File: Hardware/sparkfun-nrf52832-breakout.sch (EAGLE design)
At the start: 43 parts, among them J5 CORTEX_DEBUGPTH, U1 3.3V, U2 NRF52832, Y1 32MHz, Y2 32.768kHz

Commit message: Schematic cleanup.
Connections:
- removed net N$8: J1.DTR
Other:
- note added: "32.768kHz Crystal (RTC)"
- note added: "Buttons"
- note added: "Close JP2 & JP3 if you're attaching an NFC antenna."
- note added: "Cortex Debug Connector"
- note added: "Ctune (C7/8) = 2/((2*PI*13.56MHz)^2*La) La is inductance of NFC antenna La=1.5uH, Ctune=~180pF La=2.0uH, Ctune=~130pF"
- note added: "JP4 and JP5 enable the RTC on pins 00 and 01."
- note added: "LEDs"
- note added: "NFC Antenna Interface"
- note added: "NFC Tuning Caps"
- note added: "Pin/Supply Headers"
- note added: "Regulator Input Voltage !3.3 - 6V DC!"
- note added: "Serial Program/Debug"
- note added: "Short JP1 to enable powering the nRF52832 via a 3.3V FTDI Basic"
- note added: "Supply Decoupling"
- note added: "Voltage Regulator"
- note added: "nRF52832"
- note added: "nRF52832 Supply Range !1.7 - 3.6V DC!"
- note removed: "Ctune (C7/8) = 2/((2*PI*13.56MHz)^2*La)-4pF La is inductance of NFC antenna La=1.5uH, Ctune=~180pF La=2.0uH, Ctune=~130pF"
- moved on the sheet: C10, C11, C12, C13, C14, C15, C16, C17, C3, C4, C5, C6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

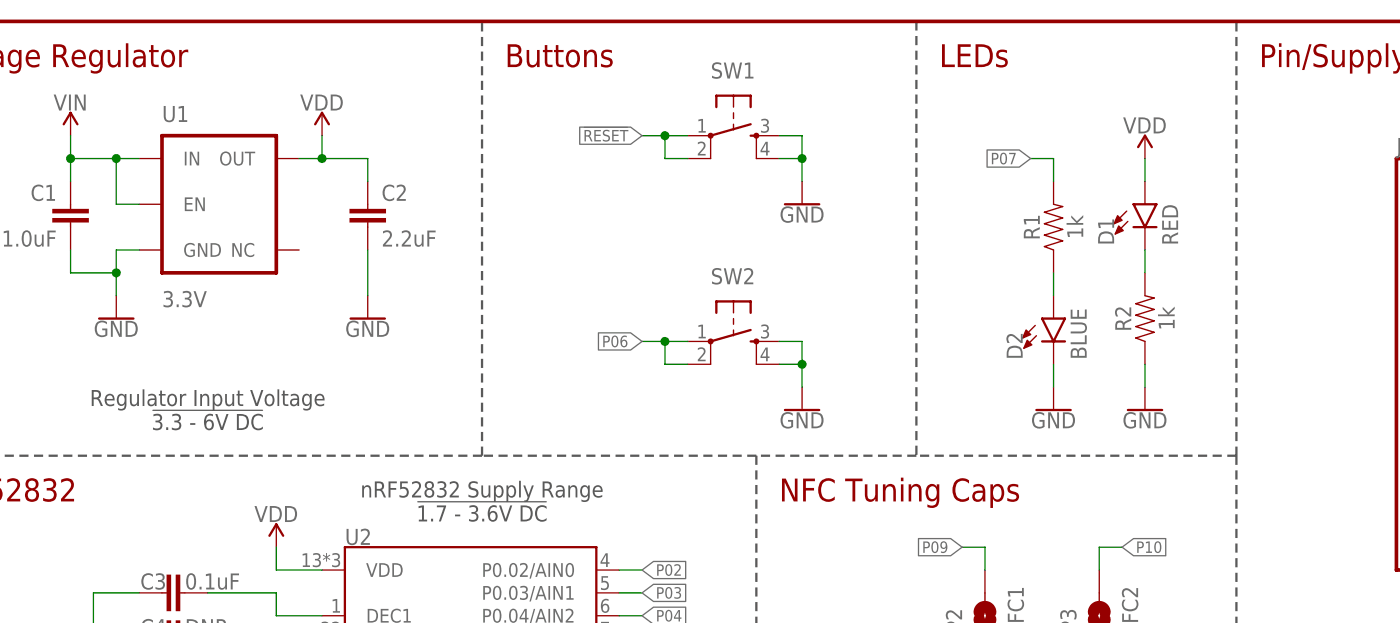
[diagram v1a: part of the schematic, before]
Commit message: Adding cut-jumper to the power LED.
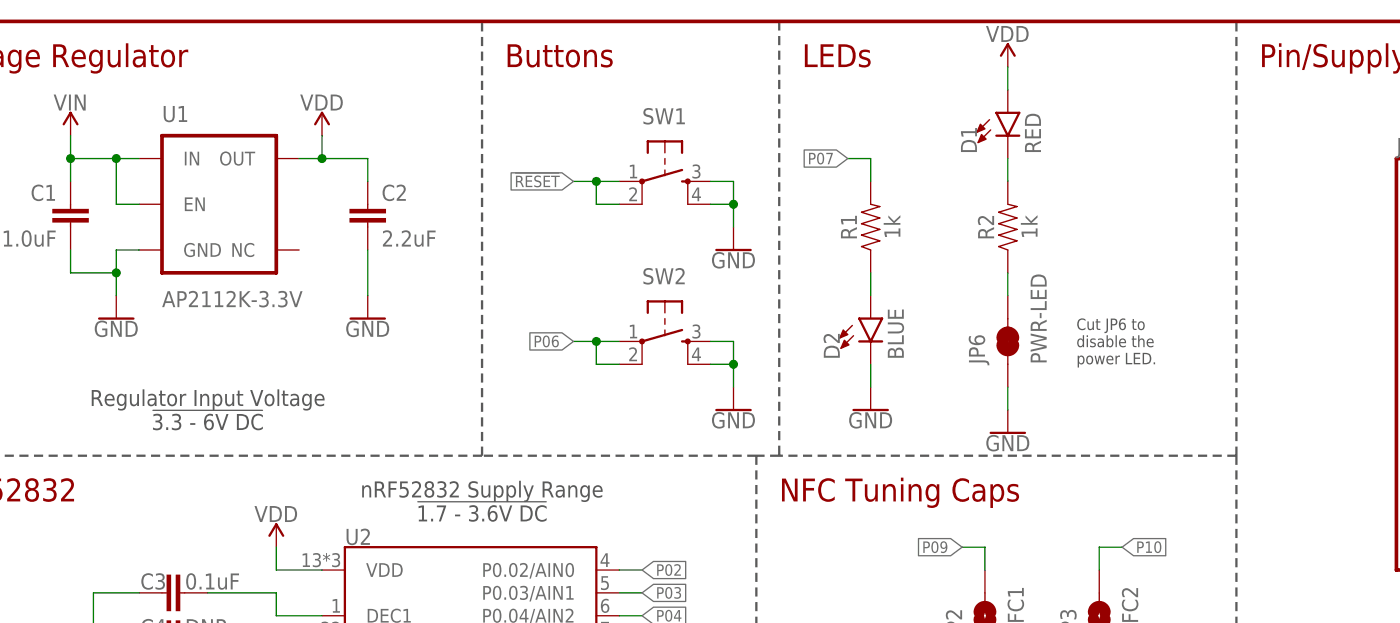
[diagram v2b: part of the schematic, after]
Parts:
- added JP6: PWR-LED, SparkFun-Jumpers:JUMPER-PAD-2-NC_BY_TRACE
- U1: value 3.3V -> AP2112K-3.3V
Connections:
- new net N$1: JP6.2, R2.1
- net GND: now also JP6.1; no longer R2.1
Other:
- note added: "Cut JP6 to disable the power LED."
- moved on the sheet: D1, D2, R1, R2, SW1, SW2

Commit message: Updates after running checklist.
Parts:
- added FD1, FD2: FIDUCIAL1X2, SparkFun-Aesthetics:FIDUCIAL1X2
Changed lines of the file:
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@@
 <part name="LOGO3" library="SparkFun-Aesthetics" deviceset="SFE_LOGO_NAME" device=".1_INCH" value="SFE_LOGO_NAME.1_INCH"/>
 <part name="JP6" library="SparkFun-Jumpers" deviceset="JUMPER-PAD-2-NC_BY_TRACE" device="" value="PWR-LED"/>
+<part name="FD1" library="SparkFun-Aesthetics" deviceset="FIDUCIAL" device="1X2"/>
+<part name="FD2" library="SparkFun-Aesthetics" deviceset="FIDUCIAL" device="1X2"/>
 </parts>
 <sheets>
@@
 <instance part="LOGO3" gate="G$1" x="86.36" y="12.7"/>
 <instance part="JP6" gate="G$1" x="121.92" y="149.86" rot="R90"/>
+<instance part="FD1" gate="G$1" x="243.84" y="20.32"/>
+<instance part="FD2" gate="G$1" x="246.38" y="17.78"/>
 </instances>
 <busses>

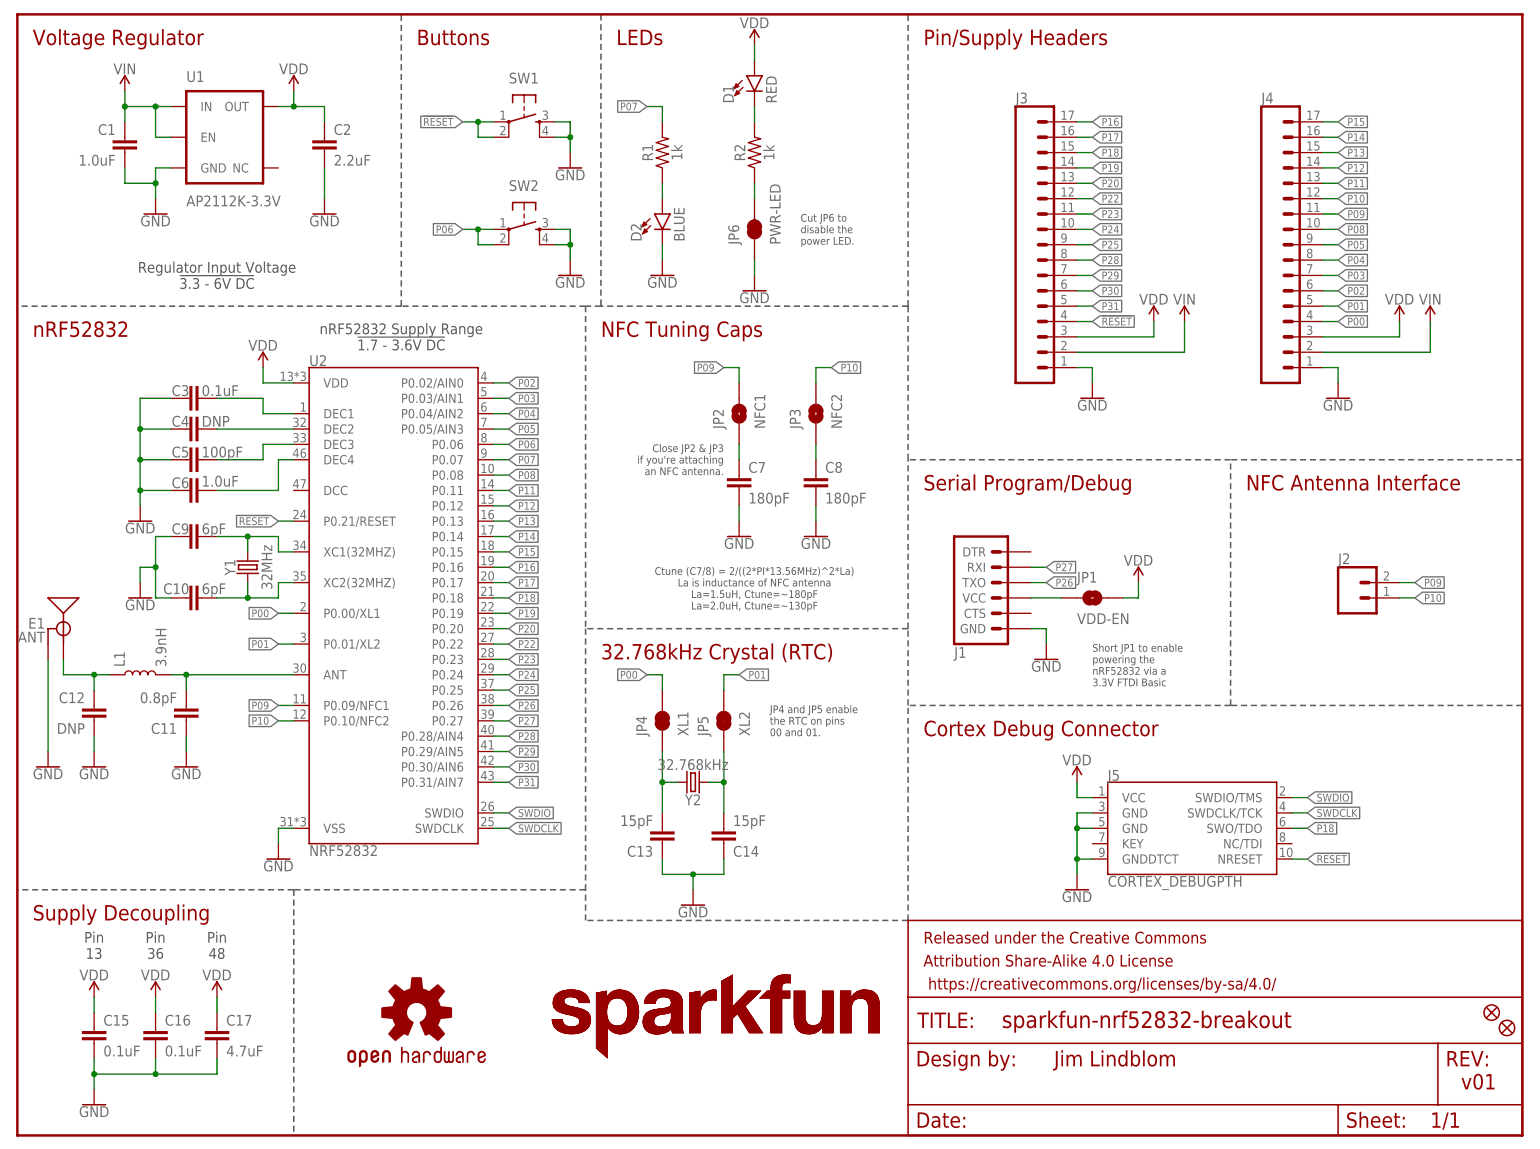
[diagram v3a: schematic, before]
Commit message: Adding test points to swd pins, stubs to NC QFN pins.
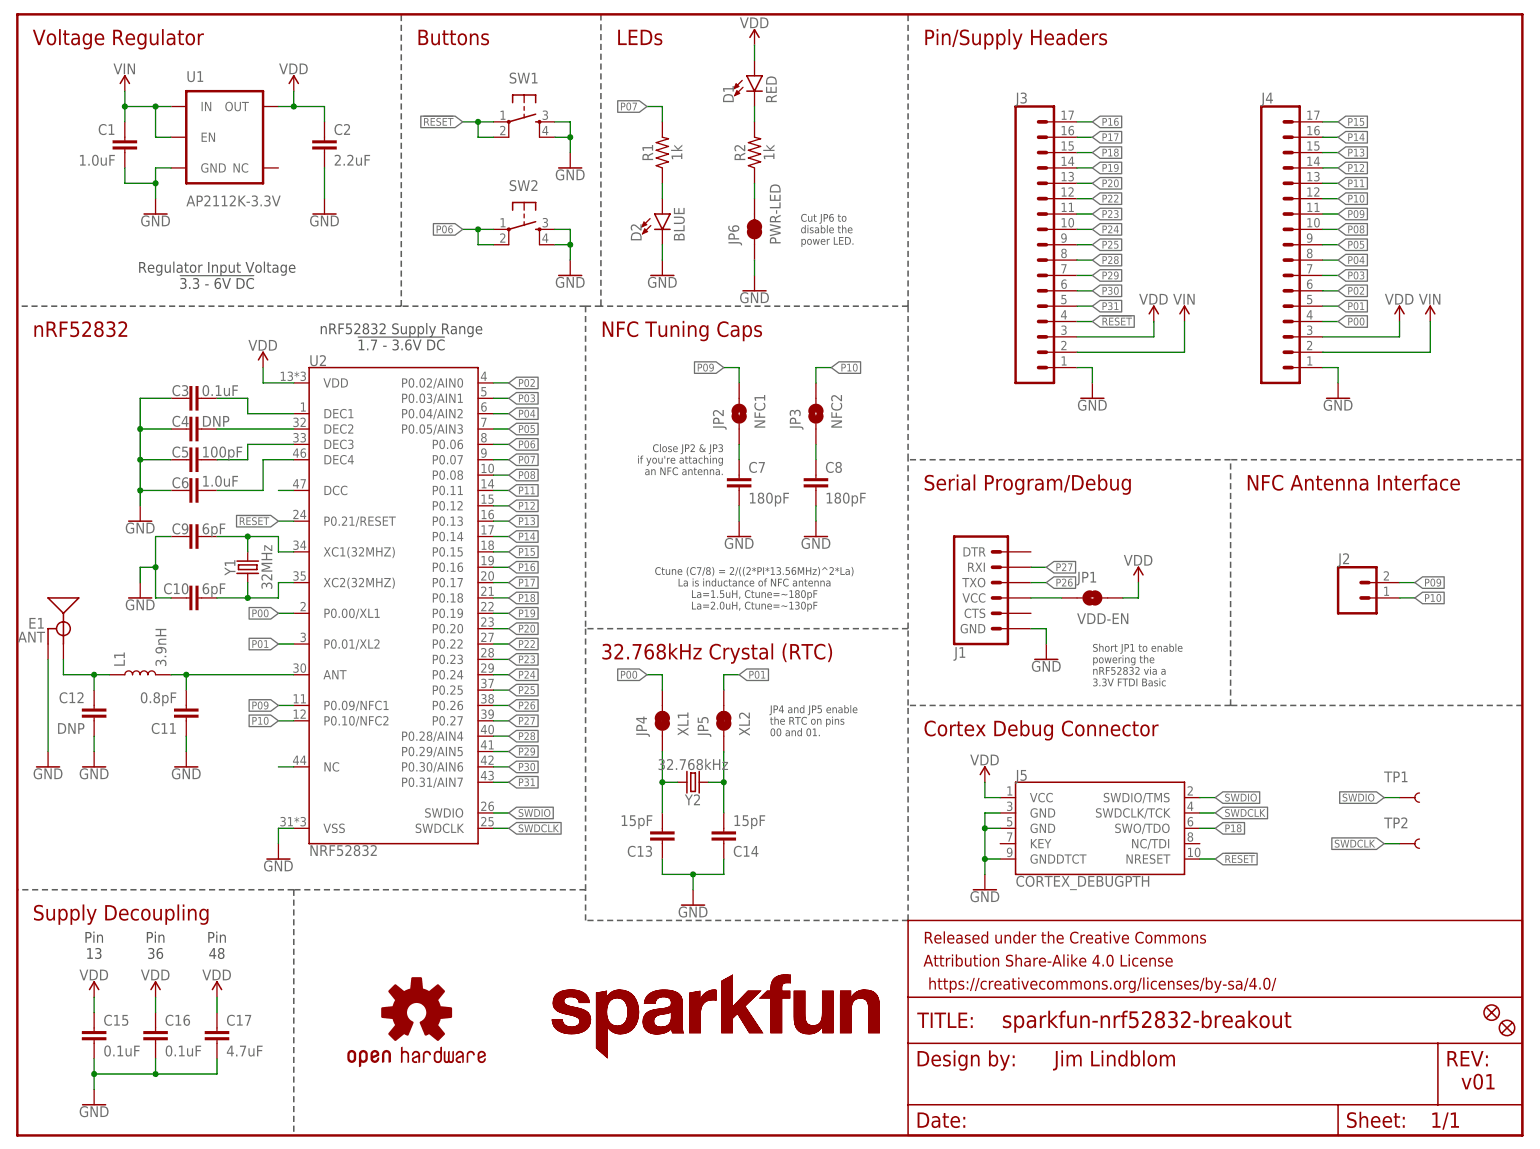
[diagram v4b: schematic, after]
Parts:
- added TP1, TP2: TEST-POINTTP_15TH_THRU, SparkFun-Connectors:TEST-POINTTP_15TH_THRU
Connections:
- new net DCC: U2.DCC
- new net NC: U2.NC
- net SWDCLK: now also TP2.1
- net SWDIO: now also TP1.1
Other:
- moved on the sheet: J5

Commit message: Moving test points to bottom, switching to micro fids, silk nudging.
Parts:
- FD1, FD2: value FIDUCIAL1X2 -> FIDUCIALUFIDUCIAL; device SparkFun-Aesthetics:FIDUCIAL1X2 -> SparkFun-Aesthetics:FIDUCIALUFIDUCIAL
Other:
- note added: "v10"
- note removed: "v01"
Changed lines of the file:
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@@
 <part name="LOGO3" library="SparkFun-Aesthetics" deviceset="SFE_LOGO_NAME" device=".1_INCH" value="SFE_LOGO_NAME.1_INCH"/>
 <part name="JP6" library="SparkFun-Jumpers" deviceset="JUMPER-PAD-2-NC_BY_TRACE" device="" value="PWR-LED"/>
-<part name="FD1" library="SparkFun-Aesthetics" deviceset="FIDUCIAL" device="1X2"/>
-<part name="FD2" library="SparkFun-Aesthetics" deviceset="FIDUCIAL" device="1X2"/>
+<part name="FD1" library="SparkFun-Aesthetics" deviceset="FIDUCIAL" device="UFIDUCIAL" value="FIDUCIALUFIDUCIAL"/>
+<part name="FD2" library="SparkFun-Aesthetics" deviceset="FIDUCIAL" device="UFIDUCIAL" value="FIDUCIALUFIDUCIAL"/>
 <part name="TP1" library="SparkFun-Connectors" deviceset="TEST-POINT" device="TP_15TH_THRU" value=""/>
 <part name="TP2" library="SparkFun-Connectors" deviceset="TEST-POINT" device="TP_15TH_THRU" value=""/>
@@
 <wire x1="147.32" y1="35.56" x2="93.98" y2="35.56" width="0.254" layer="97" style="shortdash"/>
 <wire x1="93.98" y1="35.56" x2="93.98" y2="40.64" width="0.254" layer="97" style="shortdash"/>
-<text x="238.76" y="7.62" size="2.54" layer="94" font="vector">v01</text>
+<text x="238.76" y="7.62" size="2.54" layer="94" font="vector">v10</text>
 <text x="171.45" y="11.43" size="2.54" layer="94" font="vector">Jim Lindblom</text>
 <text x="121.92" y="93.98" size="1.27" layer="97" font="vector" align="top-center">Ctune (C7/8) = 2/((2*PI*13.56MHz)^2*La)

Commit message: Making SWD test points larger drill diameter.
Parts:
- J5: device Pete_Connectors_Retired:CORTEX_DEBUGPTH -> SparkFun-Connectors:CORTEX_DEBUGPTH
- TP1, TP2: value TEST-POINTTP_15TH_THRU -> TEST-POINT3X4; device SparkFun-Connectors:TEST-POINTTP_15TH_THRU -> SparkFun-Connectors:TEST-POINT3X4
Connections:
- net !RESET!: now also J5.!RESET; no longer J5.NRESET
- net GND: no longer D2.C
- net P07: now also D2.C; no longer R1.2
- net VDD: now also R1.2
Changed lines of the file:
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@@
 <part name="GND3" library="SparkFun-PowerSymbols" deviceset="GND" device=""/>
 <part name="SUPPLY1" library="SparkFun-PowerSymbols" deviceset="VIN" device=""/>
-<part name="J5" library="Pete_Connectors_Retired" deviceset="CORTEX_DEBUG" device="PTH" value="CORTEX_DEBUGPTH"/>
+<part name="J5" library="SparkFun-Connectors" deviceset="CORTEX_DEBUG" device="PTH" value="CORTEX_DEBUGPTH"/>
 <part name="SW1" library="SparkFun-Electromechanical" deviceset="SWITCH_SPST_4_PIN" device="RECT"/>
 <part name="SW2" library="SparkFun-Electromechanical" deviceset="SWITCH_SPST_4_PIN" device="RECT"/>
@@
 <part name="R1" library="SparkFun-Resistors" deviceset="1KOHM" device="-0603-1/10W-1%" value="1k"/>
 <part name="R2" library="SparkFun-Resistors" deviceset="1KOHM" device="-0603-1/10W-1%" value="1k"/>
-<part name="GND6" library="SparkFun-PowerSymbols" deviceset="GND" device=""/>
 <part name="GND7" library="SparkFun-PowerSymbols" deviceset="GND" device=""/>
 <part name="GND1" library="SparkFun-PowerSymbols" deviceset="GND" device=""/>
@@
 <part name="FD1" library="SparkFun-Aesthetics" deviceset="FIDUCIAL" device="UFIDUCIAL" value="FIDUCIALUFIDUCIAL"/>
 <part name="FD2" library="SparkFun-Aesthetics" deviceset="FIDUCIAL" device="UFIDUCIAL" value="FIDUCIALUFIDUCIAL"/>
-<part name="TP1" library="SparkFun-Connectors" deviceset="TEST-POINT" device="TP_15TH_THRU" value=""/>
-<part name="TP2" library="SparkFun-Connectors" deviceset="TEST-POINT" device="TP_15TH_THRU" value=""/>
+<part name="TP1" library="SparkFun-Connectors" deviceset="TEST-POINT" device="3X4" value="TEST-POINT3X4"/>
+<part name="TP2" library="SparkFun-Connectors" deviceset="TEST-POINT" device="3X4" value="TEST-POINT3X4"/>
+<part name="SUPPLY14" library="SparkFun-PowerSymbols" deviceset="VDD" device=""/>
 </parts>
 <sheets>
@@
 <instance part="R1" gate="G$1" x="106.68" y="162.56" rot="R90"/>
 <instance part="R2" gate="G$1" x="121.92" y="162.56" rot="R90"/>
-<instance part="GND6" gate="1" x="106.68" y="142.24"/>
 <instance part="GND7" gate="1" x="121.92" y="139.7"/>
 <instance part="GND1" gate="1" x="91.44" y="160.02"/>
@@
 <instance part="TP1" gate="G$1" x="228.6" y="55.88"/>
 <instance part="TP2" gate="G$1" x="228.6" y="48.26"/>
+<instance part="SUPPLY14" gate="VDD" x="106.68" y="170.18"/>
 </instances>
 <busses>
@@
 </segment>
 <segment>
-<pinref part="D2" gate="G$1" pin="C"/>
-<pinref part="GND6" gate="1" pin="GND"/>
-<wire x1="106.68" y1="144.78" x2="106.68" y2="147.32" width="0.1524" layer="91"/>
-</segment>
-<segment>
 <pinref part="SW1" gate="G$1" pin="3"/>
 <wire x1="88.9" y1="167.64" x2="91.44" y2="167.64" width="0.1524" layer="91"/>
@@
 <wire x1="228.6" y1="132.08" x2="228.6" y2="134.62" width="0.1524" layer="91"/>
 </segment>
+<segment>
+<pinref part="R1" gate="G$1" pin="2"/>
+<pinref part="SUPPLY14" gate="VDD" pin="VDD"/>
+<wire x1="106.68" y1="170.18" x2="106.68" y2="167.64" width="0.1524" layer="91"/>
+</segment>
 </net>
 <net name="DEC1" class="0">
@@
 </segment>
 <segment>
-<pinref part="J5" gate="G$1" pin="NRESET"/>
+<pinref part="J5" gate="G$1" pin="!RESET"/>
 <wire x1="195.58" y1="45.72" x2="198.12" y2="45.72" width="0.1524" layer="91"/>
 <label x="198.12" y="45.72" size="1.27" layer="95" font="vector" xref="yes"/>
@@
 </segment>
 <segment>
-<pinref part="R1" gate="G$1" pin="2"/>
-<wire x1="106.68" y1="167.64" x2="106.68" y2="170.18" width="0.1524" layer="91"/>
-<wire x1="106.68" y1="170.18" x2="104.14" y2="170.18" width="0.1524" layer="91"/>
-<label x="104.14" y="170.18" size="1.27" layer="95" font="vector" rot="R180" xref="yes"/>
-</segment>
-</net>
+<pinref part="D2" gate="G$1" pin="C"/>
+<wire x1="106.68" y1="147.32" x2="106.68" y2="144.78" width="0.1524" layer="91"/>
+<wire x1="106.68" y1="144.78" x2="104.14" y2="144.78" width="0.1524" layer="91"/>
+<label x="104.14" y="144.78" size="1.27" layer="95" rot="R180" xref="yes"/>
+</segment>
+</net>

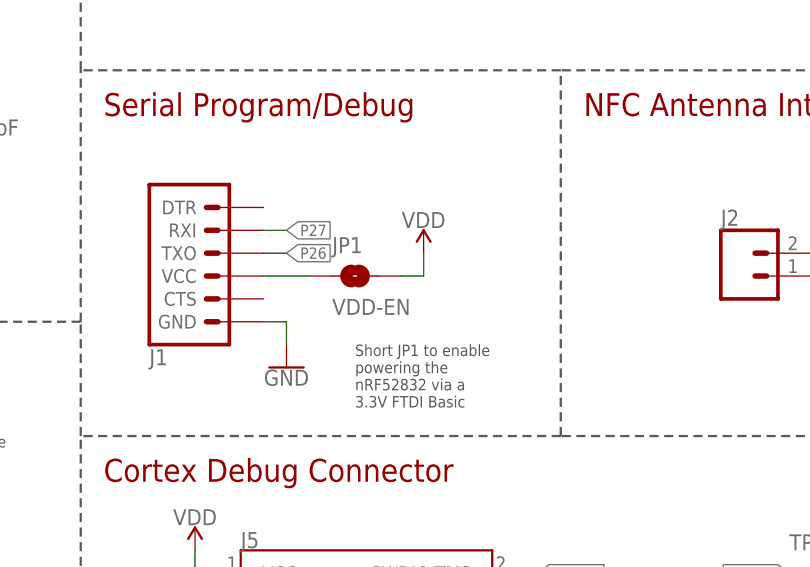
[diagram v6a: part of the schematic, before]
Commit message: Defaulting JP1 to closed.
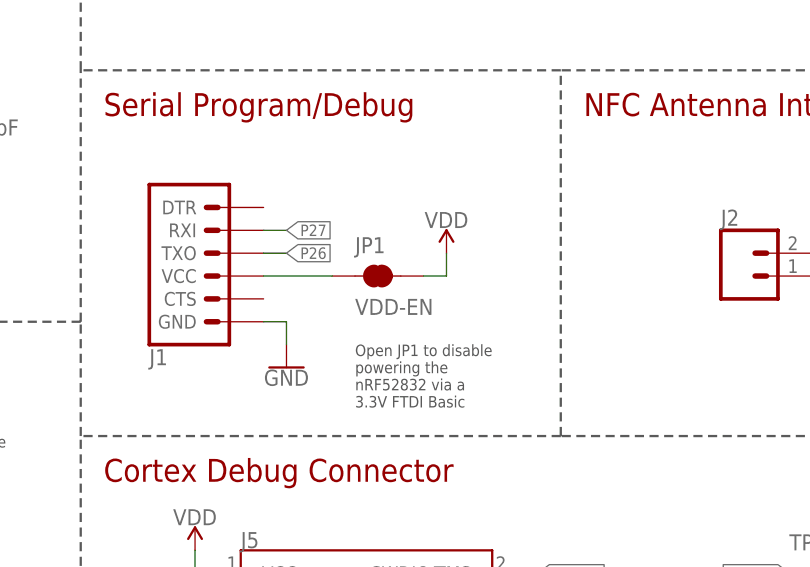
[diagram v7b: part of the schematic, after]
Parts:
- JP1: device SparkFun-Jumpers:JUMPER-PAD-2-NOYES_SILK -> SparkFun-Jumpers:JUMPER-SMT_2_NC_TRACE_SILK
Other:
- note added: "Open JP1 to disable powering the nRF52832 via a 3.3V FTDI Basic"
- note removed: "Short JP1 to enable powering the nRF52832 via a 3.3V FTDI Basic"
